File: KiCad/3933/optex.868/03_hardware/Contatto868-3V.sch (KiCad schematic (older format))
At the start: 23 parts, among them CN3 STRIP Prog., P1 SERIAL CONNECTOR, P2 JBAT, P3 TAMPER CONNECTOR, Q1 Q_NMOS_DGS, U2 MSP430G2433IRHN32

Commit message: Kicad and firmware updates
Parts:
- P2: footprint saet:3v6_saft_battery_holder -> saet:molex_22-03-5025
- Q1: symbol Q_NMOS_DGS -> Q_NMOS_GSD
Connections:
- net TX: now also Q1.2 (S); no longer Q1.3 (S)
- net Yellow: now also Q1.3 (D); no longer Q1.1 (D)
- net at R2.1: now also Q1.1 (G); no longer Q1.2 (G)
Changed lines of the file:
@@
-$EndComp
-$Comp
-L LED DL1
-U 1 1 53F31549
-P 8300 2750
-F 0 "DL1" H 8300 2850 59  0000 C CNN
-F 1 "LEDR-LHN974" H 8350 2600 59  0000 C CNN
-F 2 "LEDs:LED_0805" H 8300 2750 60  0001 C CNN
-F 3 "~" H 8300 2750 60  0000 C CNN
-F 4 "LE7011" H 8300 2750 60  0001 C CNN "Saet_code"
-	1    8300 2750
-	-1   0    0    -1
 $EndComp
 $Comp
@@
 NoConn ~ 5700 4350
 $Comp
-L Q_NMOS_DGS Q1
+L Q_NMOS_GSD Q1
 U 1 1 5BA24173
 P 3750 4400
@@
 F 0 "P2" H 1850 1400 50  0000 C CNN
 F 1 "JBAT" V 1950 1250 50  0000 C CNN
-F 2 "saet:3v6_saft_battery_holder" H 1850 1250 50  0000 C CNN
+F 2 "saet:molex_22-03-5025" H 1850 1250 50  0000 C CNN
 F 3 "" H 1850 1250 50  0000 C CNN
 F 4 "WK1011" H 1850 1250 60  0001 C CNN "Saet_code"
@@
 Wire Notes Line
 	750  5350 750  4300
+$Comp
+L LED DL1
+U 1 1 5C13868D
+P 8300 2750
+F 0 "DL1" H 8300 2850 50  0000 C CNN
+F 1 "LEDR-LHN974" H 8300 2650 50  0000 C CNN
+F 2 "LEDs:LED_0805" H 8300 2950 60  0000 C CNN
+F 3 "" H 8300 2750 60  0000 C CNN
+F 4 "LE7011" H 8300 2750 60  0001 C CNN "Saet_code"
+	1    8300 2750
+	-1   0    0    -1
+$EndComp
 $EndSCHEMATC

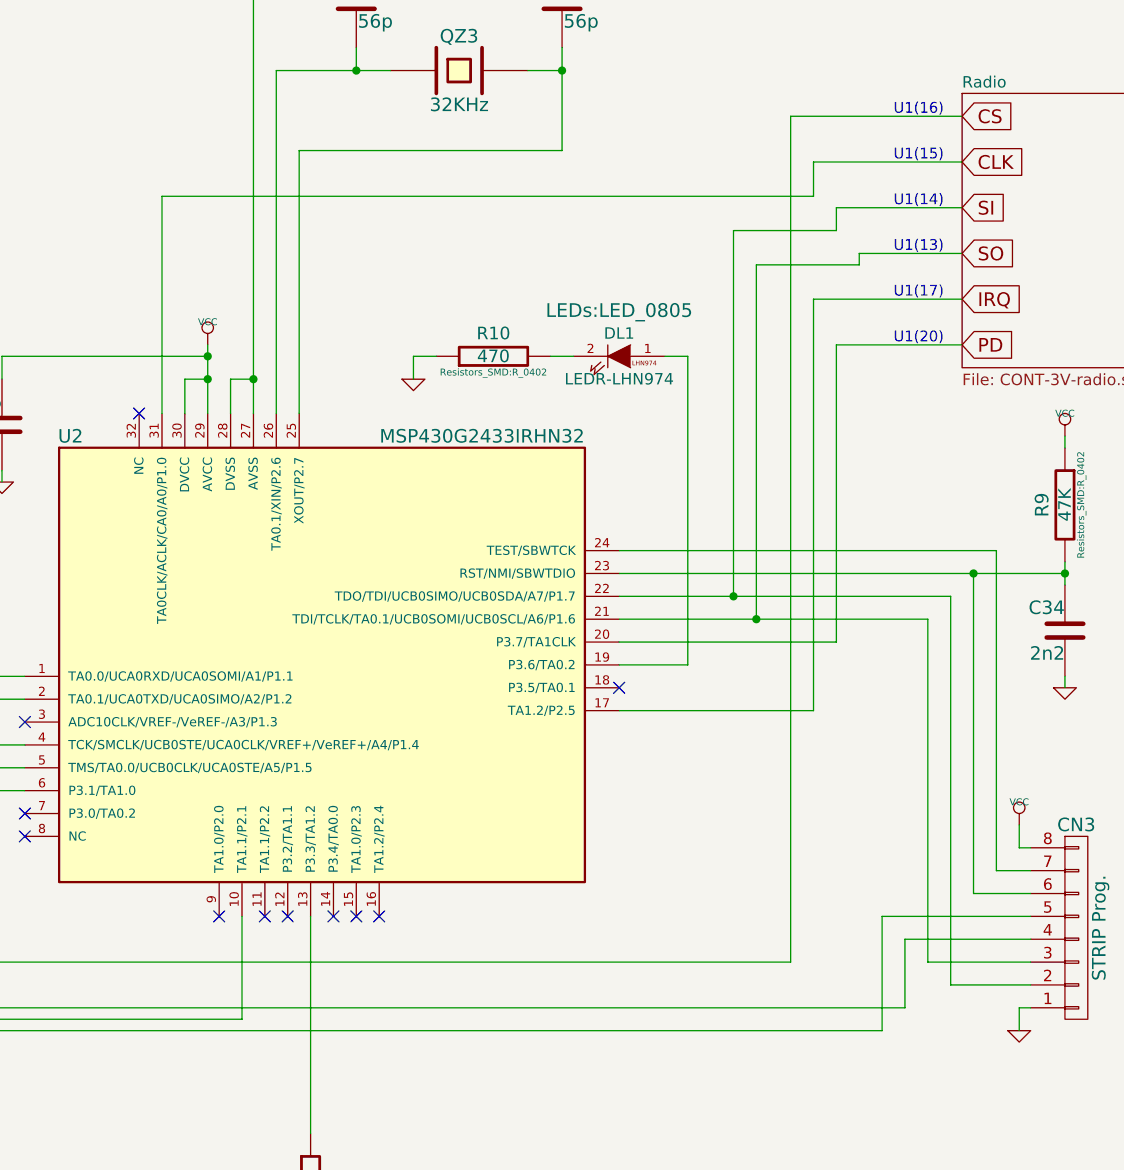
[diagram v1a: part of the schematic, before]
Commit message: Aggiornamenti su modulo SPI (sw->hw) e vari sui circuiti
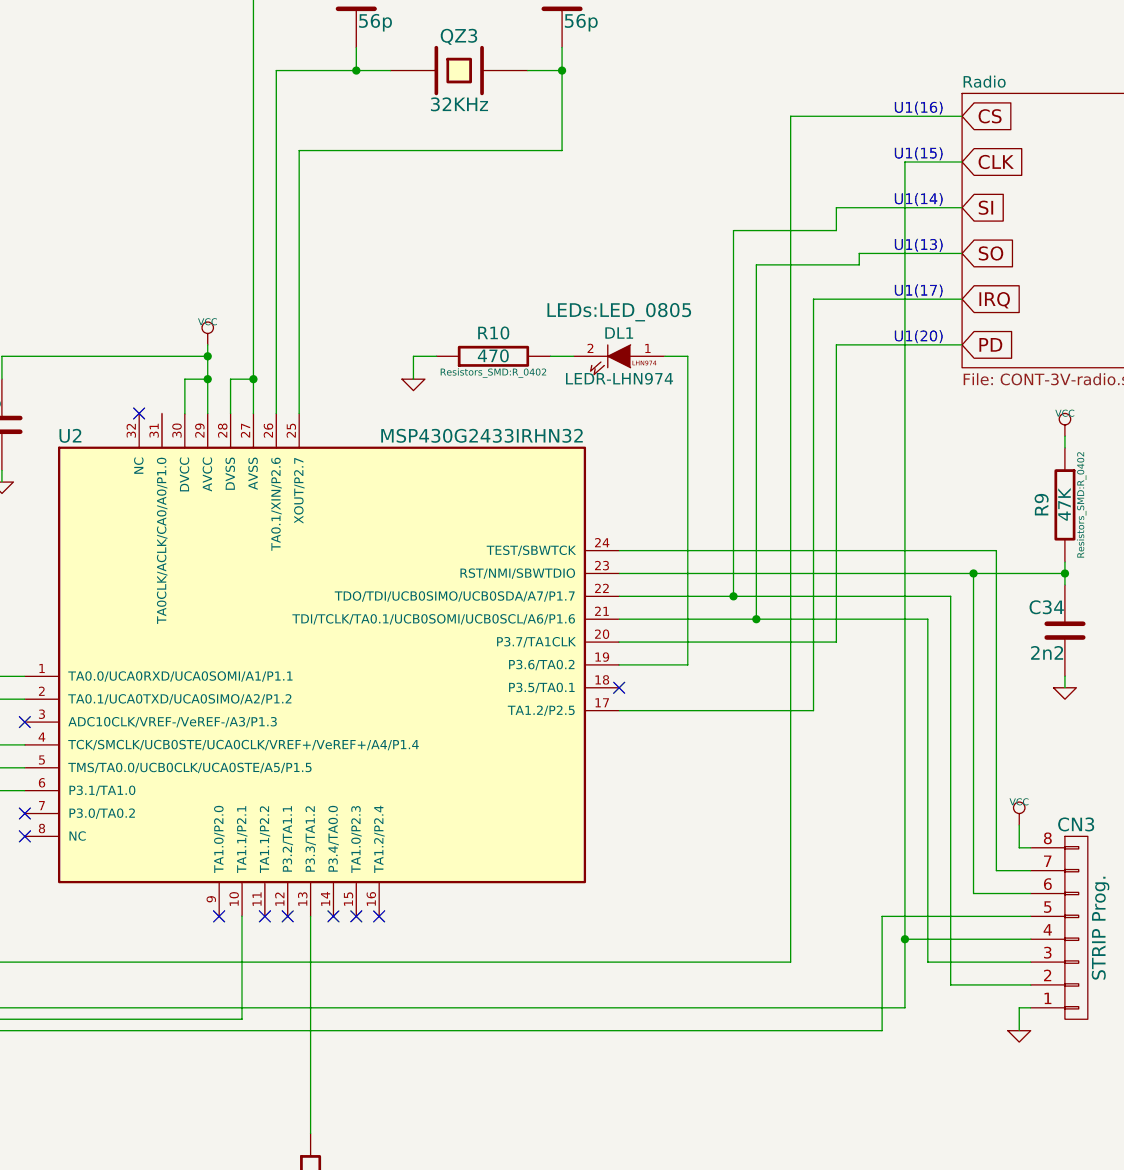
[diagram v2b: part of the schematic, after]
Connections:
- net CLK: now also CN3.4 (P4), U2.5 (TMS/TA0.0/UCB0CLK/UCA0STE/A5/P1.5); no longer U2.31 (TA0CLK/ACLK/CA0/A0/P1.0)
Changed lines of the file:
@@
 	9450 5700 5100 5700
 Wire Wire Line
-	9550 5300 9550 5600
+	9550 1900 9550 5600
 Wire Wire Line
 	9550 5600 5200 5600
@@
 	9800 1700 9050 1700
 Wire Wire Line
-	6300 3000 6300 2050
-Wire Wire Line
 	10100 5600 10050 5600
 Wire Wire Line
@@
 Wire Wire Line
 	8600 2750 8500 2750
-Wire Wire Line
-	9150 2050 9150 1900
-Wire Wire Line
-	9150 1900 9800 1900
 Wire Wire Line
 	9250 2200 9250 2100
@@
 Wire Wire Line
 	7400 2750 7400 2850
-Wire Wire Line
-	6300 2050 9150 2050
 Wire Wire Line
 	8900 2350 8900 3900
@@
 	-1   0    0    -1
 $EndComp
+Wire Wire Line
+	9800 1900 9550 1900
+Connection ~ 9550 5300
 $EndSCHEMATC
